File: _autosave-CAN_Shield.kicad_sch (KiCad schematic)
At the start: 16 parts, among them J1 GPIO, U1 MX128-5.08-09P-GN01-CU-Y-A, U2 MCP2515T-I/SO, U4 SN65HVD230DR, X1 X322516MLB4SI

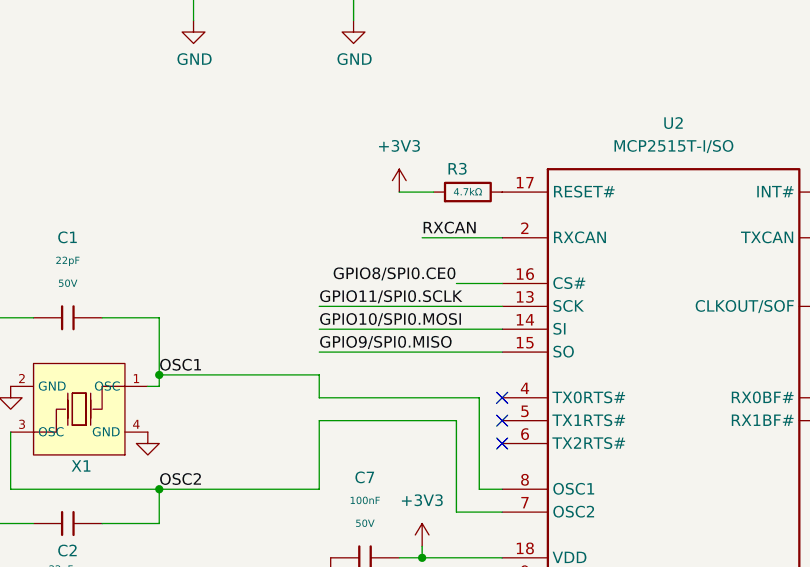
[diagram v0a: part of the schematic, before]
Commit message: change can diff pair trace width to 0.35 mm get 133ohm zdiff
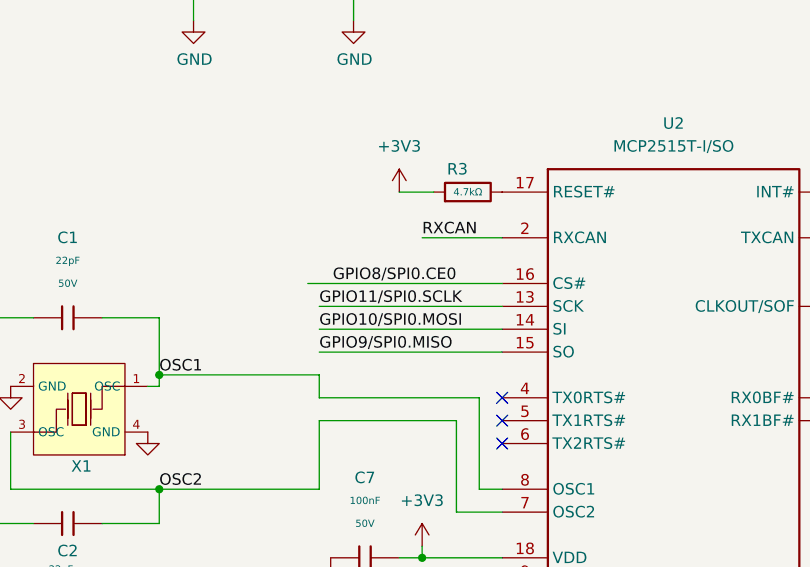
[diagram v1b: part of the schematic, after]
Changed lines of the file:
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@@
+	(wire
+		(pts
+			(xy 121.92 110.49) (xy 125.73 110.49)
+		)
+		(stroke
+			(width 0)
+			(type default)
+		)
+	)
 	(wire
 		(pts
@@
 	(wire
 		(pts
-			(xy 121.92 110.49) (xy 125.73 110.49)
-		)
-		(stroke
-			(width 0)
-			(type default)
-		)
-	)
-	(wire
-		(pts
 			(xy 22.86 41.91) (xy 52.07 41.91)
 		)
@@
 	(wire
 		(pts
-			(xy 78.74 115.57) (xy 83.82 115.57)
-		)
-		(stroke
-			(width 0)
-			(type default)
-		)
-	)
-	(wire
-		(pts
 			(xy 22.86 72.39) (xy 52.07 72.39)
 		)
@@
 		)
 	)
+	(wire
+		(pts
+			(xy 62.23 115.57) (xy 83.82 115.57)
+		)
+		(stroke
+			(width 0)
+			(type default)
+		)
+	)
